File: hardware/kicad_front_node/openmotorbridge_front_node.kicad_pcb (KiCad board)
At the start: 4 copper layers, 82 x 50 mm, 64 parts, among them J1 JST_GH_04P_BACKBONE, J10 JST_PH_02P_NAVI_PWR, J4 JST_GH_06P_HUB_EXT, J8 JST_PH_02P_CAM_PWR, Q1 DMN63D8_BSD_MOSFET, Q2 TPS1H100_AUX_LIGHT, SW1 BOOT, SW2 RESET, U1 ESP32-P4-NR16, U2 USB2514Bi-AEZG, U3 TPS54302_5V_BUCK, U4 TPS2051B_PORT2_GATE, U5 SW3526_USB_PD1_30W, U7 TLV75533P_3V3_LDO, U9 ESP32-E22-WROOM-2X2, Y1 24.000MHz

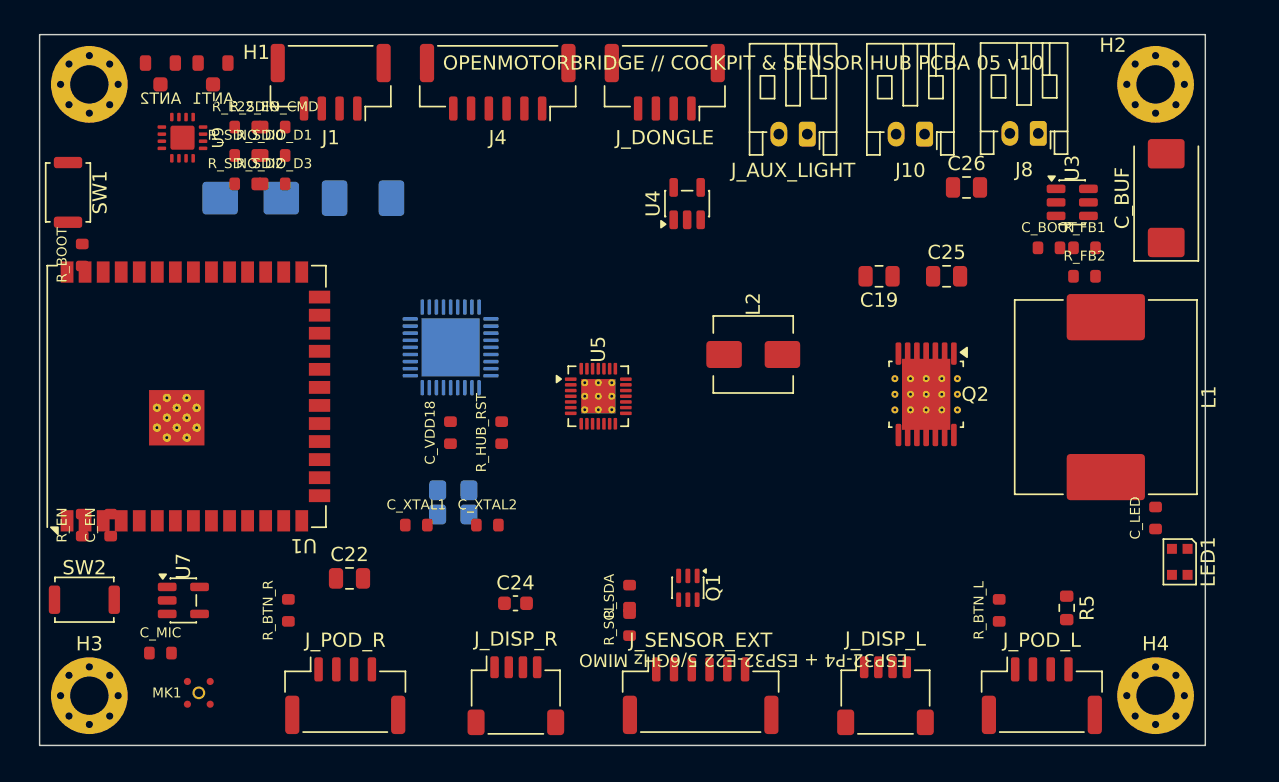
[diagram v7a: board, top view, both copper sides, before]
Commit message: feat(hardware): finalize Front Node PCBA 05 routing, net assignments, planes, and schematic parity
- Resolved all 0 unconnected items and cleared shorts on Front Node PCB
- Assigned nets across all 41 pins of U1, U5, Q2, LED1, and JST connectors
- Created and filled continuous GND and VCC_3V3 planes on In1.Cu and In2.Cu
- Synchronized KiCad schematic 1:1 to PCB achieving 0 blockers in prefab-gate check
- Removed obsolete CAN transceiver references from Front Node documentation
- Updated 3D renders for PCBA 05 top and bottom views in docs/images/pcba/
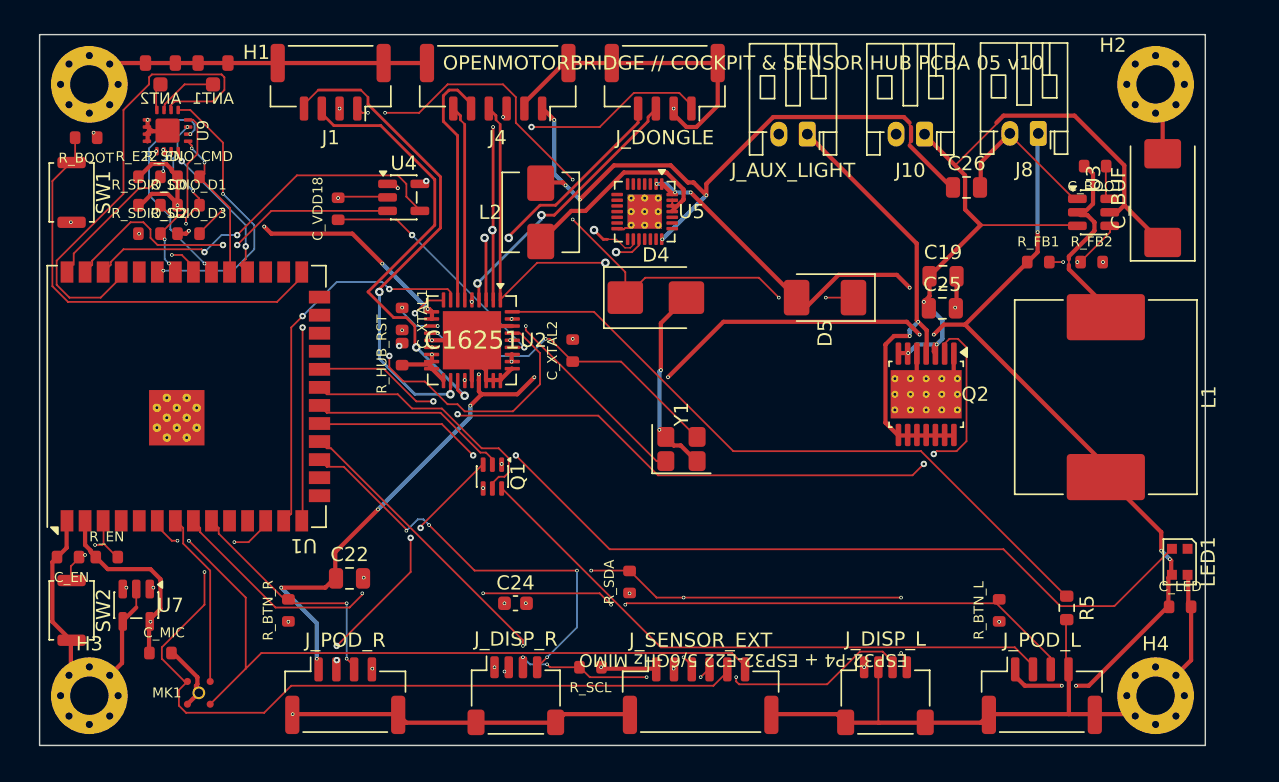
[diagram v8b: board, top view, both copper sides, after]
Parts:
- C24: footprint C_0603_1608Metric -> Capacitor_SMD:C_0603_1608Metric
- D4, D5, U2, Y1: moved to F.Cu
- R5: footprint R_0603_1608Metric -> Resistor_SMD:R_0603_1608Metric
- moved D5 33.2 mm to (155.2, 88.5), turned to 180 degrees
- moved D4 29.3 mm to (143.3, 88.5), turned to 0 degrees
- moved U4 19.9 mm to (125.6, 81.5), turned to 0 degrees
- moved L2 18.0 mm to (135.2, 82.5), turned to 90 degrees
- moved C_VDD18 17.6 mm to (121.0, 82.2)
- moved Y1 16.5 mm to (145.2, 99.2), turned to 0 degrees
- moved Q1 15.8 mm to (131.8, 101.1)
- moved C_XTAL1 14.5 mm to (125.5, 90.0), turned to -90 degrees
- moved C_XTAL2 13.7 mm to (137.5, 92.2), turned to 90 degrees
- moved U5 13.4 mm to (142.6, 82.5), turned to -90 degrees
- moved R_HUB_RST 8.92 mm to (125.5, 92.5)
- moved R_BOOT 8.25 mm to (103.3, 77.2), turned to 180 degrees
- moved R_E22_EN 7.63 mm to (107.7, 80.0)
- moved R_SDIO_D0 7.63 mm to (107.7, 82.0)
- moved R_SDIO_D2 7.63 mm to (107.7, 84.0)
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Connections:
- LED1 pad 1: (no net) -> LED1_DOUT
- Q2 pad : (no net) -> GND
- Q2 pad 10: (no net) -> +12V_AUX
- Q2 pad 11: (no net) -> +12V_AUX
- Q2 pad 12: (no net) -> +12V_AUX
- Q2 pad 13: (no net) -> +12V_AUX
- Q2 pad 14: (no net) -> +12V_AUX
- Q2 pad 6: (no net) -> +12V_PROT
- Q2 pad 7: (no net) -> +12V_PROT
- Q2 pad 8: (no net) -> +12V_AUX
- Q2 pad 9: (no net) -> +12V_AUX
- U1 pad : (no net) -> GND
- U1 pad 10: (no net) -> GPIO10
- U1 pad 11: (no net) -> GPIO11
- U1 pad 15: (no net) -> GPIO15
- U1 pad 16: (no net) -> GPIO16
- U1 pad 23: (no net) -> GPIO23
- U1 pad 24: (no net) -> GPIO24
- U1 pad 25: (no net) -> GPIO25
- U1 pad 26: (no net) -> GPIO26
- U1 pad 28: (no net) -> GPIO28
- U1 pad 29: (no net) -> GPIO29
- U1 pad 36: (no net) -> GPIO36
- U1 pad 4: (no net) -> GPIO4
- U1 pad 5: (no net) -> GPIO5
- U2 pad : (no net) -> GND
- U5 pad : (no net) -> GND
- U5 pad 10: (no net) -> U5_NC10
- U5 pad 11: (no net) -> U5_NC11
- U5 pad 12: (no net) -> U5_NC12
- U5 pad 13: (no net) -> U5_NC13
- U5 pad 14: (no net) -> GND
- U5 pad 15: (no net) -> U5_NC15
- U5 pad 16: (no net) -> USB_DN1_DP
- U5 pad 17: (no net) -> USB_DN1_DM
- U5 pad 18: (no net) -> USB_DN1_CC1
- U5 pad 19: (no net) -> USB_DN1_CC2
- U5 pad 2: SW_PD1_BUCK -> +12V_PROT
- U5 pad 20: (no net) -> U5_NC20
- U5 pad 21: (no net) -> VBUS_PD1_OUT
- U5 pad 22: (no net) -> U5_NC22
- U5 pad 23: (no net) -> U5_NC23
- U5 pad 24: (no net) -> U5_NC24
- U5 pad 25: (no net) -> SW_PD1_BUCK
- U5 pad 26: (no net) -> SW_PD1_BUCK
- U5 pad 27: (no net) -> SW_PD1_BUCK
- U5 pad 28: (no net) -> +12V_PROT
- U5 pad 3: VBUS_PD1_OUT -> U5_BST
- U5 pad 4: GND -> U5_SW_SN
- U5 pad 5: USB_DN1_CC1 -> U5_NC5
- U5 pad 6: USB_DN1_CC2 -> U5_NC6
- U5 pad 7: USB_DN1_DP -> U5_NC7
- U5 pad 8: USB_DN1_DM -> U5_NC8
- U5 pad 9: (no net) -> U5_NC9
- U7 pad 4: (no net) -> GND
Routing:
- net GND: track 0.00 -> 196.4 mm, vias 0 -> 21
- net VCC_5V: track 0.00 -> 150.0 mm, vias 0 -> 17
- net +12V_PROT: track 0.00 -> 78.5 mm, vias 0 -> 7
- net WS2812B_DIN: track 0.00 -> 67.0 mm, vias 0 -> 2
- net BTN_SIG_L_N: track 0.00 -> 66.7 mm, vias 0 -> 4
- net I2C_SDA: track 0.00 -> 64.1 mm, vias 0 -> 9
- net AUX_LIGHT_EN: track 0.00 -> 58.9 mm, vias 0 -> 4
- net MIC_I2S_DATA: track 0.00 -> 58.0 mm, vias 0 -> 2
- net VCC_3V3: track 0.00 -> 55.0 mm, vias 0 -> 23
- net MIC_I2S_WS: track 0.00 -> 53.4 mm, vias 0 -> 2
- net I2C_SCL: track 0.00 -> 51.6 mm, vias 0 -> 6
- net VBUS_PD1_OUT: track 0.00 -> 47.9 mm, vias 0 -> 5
- net HUB_RBIAS: track 0.00 -> 47.4 mm
- net VIN_60W: track 0.00 -> 47.0 mm, vias 0 -> 6
- net BSD_LED_L_N: track 0.00 -> 42.9 mm
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- added copper zone on In1.Cu, net GND
- added copper zone on In2.Cu, net VCC_3V3
